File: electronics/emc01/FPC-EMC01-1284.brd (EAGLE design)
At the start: 100 x 86.6 mm, 52 parts, among them IC1 FT232RL, J10 ICSP, J11 CONN-RECT-16PIN-2ROW, J12 CONN-RECT-16PIN-2ROW, J13 CONN-RECT-16PIN-2ROW, J14 CONN-RECT-16PIN-2ROW, J2 PCIE, J4 MOT-X, J5 MOT-Y, J6 MOT-Z, J7 CONN-RECT-3PINJST_PH_2MM, J8 CONN-RECT-3PINJST_PH_2MM, J9 CONN-RECT-3PINJST_PH_2MM, Q4 16Mhz, U1 STEPSTICK, U2 STEPSTICK, U3 STEPSTICK, U5 ATMEGA1284P-AU, U6 LM2576-D2T, X1 USB-MICROB

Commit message: some extra routing
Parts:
- moved LED2 72.7 mm to (55.9, 8.35), turned to 270 degrees
- moved R6 70.2 mm to (55.9, 10.2), turned to 0 degrees
- moved JP5 1.60 mm to (90.9, 50.2)
- moved C18 1.57 mm to (84.2, 49.4)
- moved C36 0.86 mm to (39.1, 52.0)
- moved C34 0.70 mm to (39.2, 49.8)
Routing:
- net TOOL4_AIN: track 0.00 -> 125.6 mm, vias 0 -> 2
- net TOOL4_ENABLE: track 0.00 -> 84.0 mm, vias 0 -> 2
- net !RESET: track 90.8 -> 145.1 mm, vias 3 -> 4
- net SCLK: track 19.7 -> 73.6 mm, vias 0 -> 2
- net TOOL_DIR: track 27.6 -> 80.4 mm, vias 0 -> 3
- net TOOL4_DOUT: track 0.00 -> 40.1 mm, vias 0 -> 3
- net SDA: track 101.8 -> 133.5 mm
- net MISO: track 46.0 -> 76.4 mm, vias 1 -> 2
- net TOOL3_AIN: track 22.2 -> 52.5 mm, vias 1 -> 3
- net !XYZ-ENABLE: track 23.7 -> 44.9 mm, vias 0 -> 1
- net SCL: track 163.7 -> 181.7 mm, vias 3 -> 4
- net TOOL1_AIN: track 0.00 -> 3.78 mm
- net 12V: track 221.9 -> 219.8 mm
- net N$2: track 0.00 -> 1.91 mm
- net AVR_TXD: track 138.6 -> 139.9 mm
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
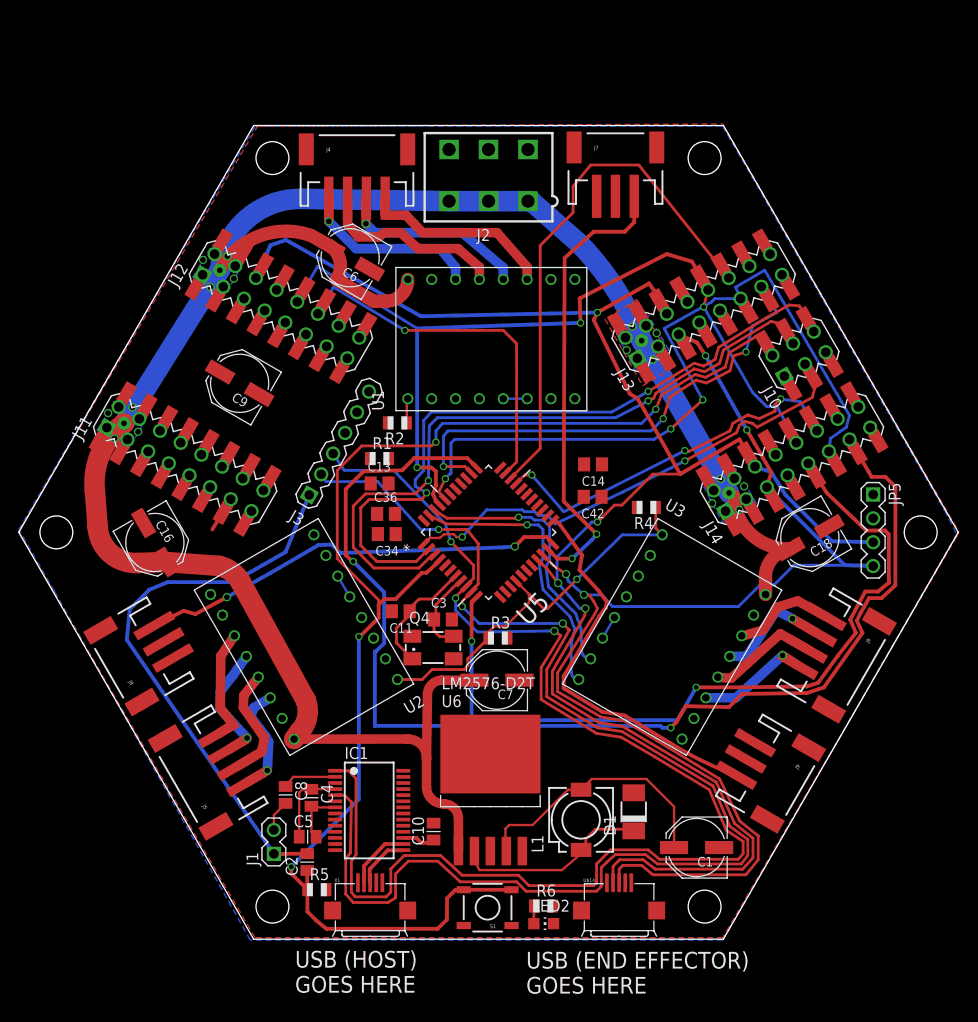
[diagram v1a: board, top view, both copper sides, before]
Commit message: - Swapped FT232RL for FT231XS (copied/pasted to Sparkfun RedBoard) - Replaced micro USB with mini USB - Deleted second micro USB and Z probe pin (we can use a modular connector Z probe instead rather than having a special connector for it)
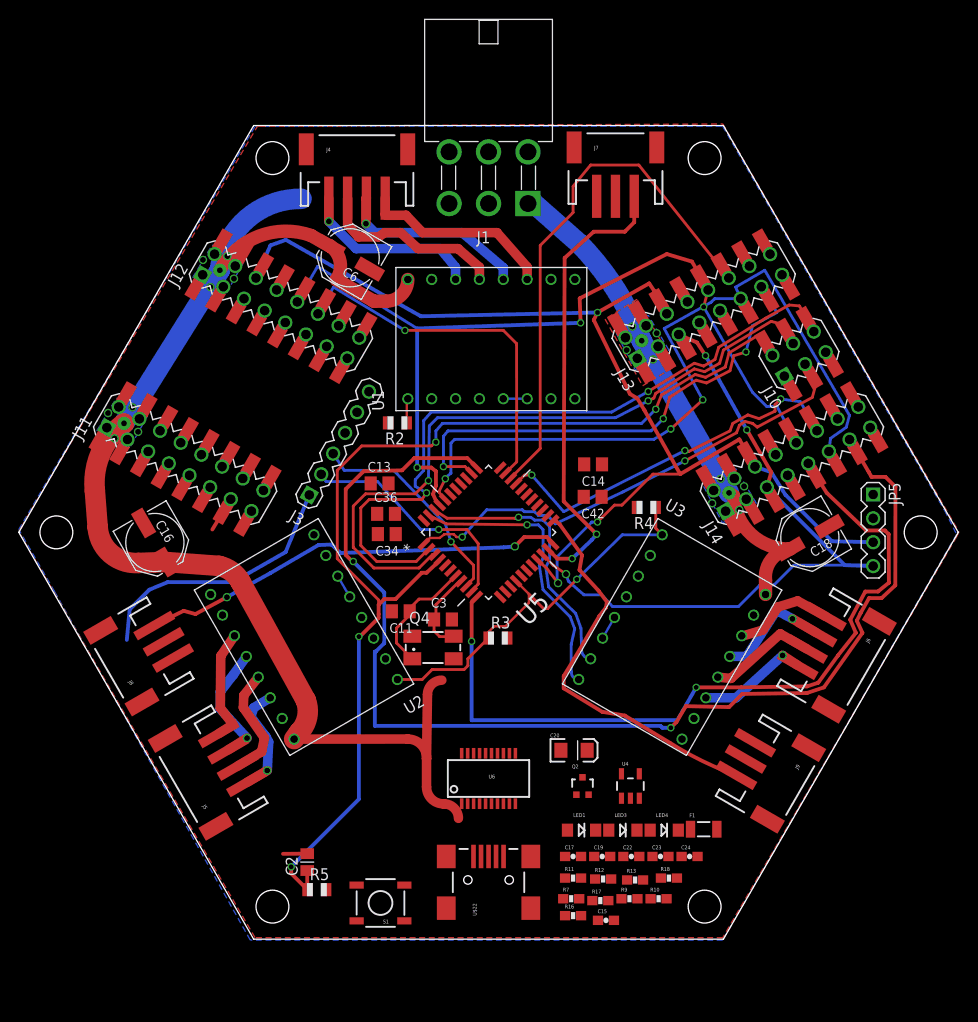
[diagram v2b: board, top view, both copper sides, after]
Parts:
- removed C1: 470uF, rcl:PANASONIC_D
- removed C10, C5, C8: 0.1uF, ipc-7351-capacitor:CAPC2012X145AN
- removed C4: 0.33uF, ipc-7351-capacitor:CAPC2012X145AN
- removed C7, C9: 100uF, rcl:PANASONIC_D
- removed D1: (no value), diode:DO-214AC
- removed IC1: FT232RL, ftdichip:SSOP28
- removed J2: PCIE, printrbot:5566-6
- removed L1: SLF7045, inductors:SLF7045
- removed LED2: PWR, led:CHIP-LED0805
- removed R1: 10K, adafruit:R0805
- removed R6: 330, adafruit:R0805
- removed U$14: USB-MICROB-I2CUSB-, SparkFun:USB-MICROB-I2C
- removed X1: USB-MICROB, SparkFun:USB-MICROB
- added C15: 1uF, SparkFun:0603-CAP
- added C17, C19, C24: 0.1uF, SparkFun:0603-CAP
- added C20: 10uF, SparkFun-Capacitors:EIA3216
- added C22, C23: 47pF, SparkFun-Capacitors:0603-CAP
- added F1: 500mA, SparkFun:PTC-1206
- added LED1: Green, SparkFun-LED:LED-1206-NO_SILK
- added LED3: Red, SparkFun-LED:LED-1206-NO_SILK
- added LED4: Yellow, SparkFun-LED:LED-1206-NO_SILK
- added Q2: 2N7002PW, SparkFun-DiscreteSemi:SOT323
- added R10, R11, R12, R7, R9: 1k, SparkFun:0603-RES
- added R13, R16: 27, SparkFun-Resistors:0603-RES
- added R17, R18: 10k, SparkFun:0603-RES
- added U$22: USB-MINIB-5PIN, SparkFun-Connectors:USB-MINIB
- added U4: MIC5205, SparkFun:SOT23-5
- J1: value (none) -> CONN-MOLEX-MICROFIT-6PIN; device !con-lstb:MA02-1 -> FirePick:CONN-MOLEX-MINIFIT-6PIN-2ROW
- U6: value LM2576-D2T -> FT231XS; device FirePick:D2PAK -> SparkFun-DigitalIC:SSOP20_L
- moved J1 71.7 mm to (50.0, 85.0), turned to 0 degrees
- moved S1 11.4 mm to (38.5, 10.6)
- moved U6 2.61 mm to (50.0, 23.8)
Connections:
- removed net N$10: C8.2, J1.2
- removed net N$12: C10.1, IC1.17
- removed net N$2: LED2.A, R6.1
- removed net N$3: C8.1, IC1.2
- removed net N$5: C1.+, L1.2, U6.4
- removed net USB_D+: IC1.15, X1.D+
- removed net USB_D-: IC1.16, X1.D-
- removed net Z-PROBE: R1.2, U5.44
- new net 3.3V: C15.1, C24.1, Q2.1, R17.2, U4.5, U6.13, U6.14, U6.3
- new net D+: C22.1, R16.1, U$22.D+
- new net D-: C23.1, R13.1, U$22.D-
- new net N$21: LED3.A, R9.2
- new net N$22: LED4.A, R10.2
- new net N$23: R13.2, U6.12
- new net N$25: R16.2, U6.11
- new net N$26: Q2.2, R17.1, U6.1
- new net RESERVED: U5.44
- new net RXD: R12.2, U6.4
- new net RXLED: LED4.C, U6.17
- new net TXD: R11.2, U6.20
- new net TXLED: LED3.C, U6.10
- new net VUSB: C17.1, F1.1, U$22.VBUS
- net +5V: now also C19.1, C20.A, F1.2, R10.1, R18.2, R7.2, R9.1, U4.1, U4.3, U6.15; no longer C4.1, C5.1, IC1.20, IC1.4, R1.1, R6.2, U$14.+5V
- net 12V: now also J1.1, J1.2, J1.3; no longer C7.+, C9.+, J2.1, J2.2, J2.3, U6.1
- net AVR_RXD: now also R11.1; no longer IC1.1
- net AVR_TXD: now also R12.1; no longer IC1.5
- net DTR: now also Q2.3, R18.1; no longer J1.1
- net GND: now also C15.2, C17.2, C19.2, C20.C, C22.2, C23.2, C24.2, J1.4, J1.5, J1.6, LED1.C, U$22.GND, U$22.MTN1, U$22.MTN2, U$22.MTN3, U$22.MTN4, U4.2, U6.16; no longer C1.-, C10.2, C4.2, C5.2, C7.-, C9.-, D1.A, IC1.18, IC1.21, IC1.25, IC1.26, IC1.7, J2.4, J2.5, J2.6, LED2.C, U$14.GND, U6.3, U6.5, X1.GND
- net N$4: now also LED1.A, R7.1; no longer D1.C, L1.1, U6.2
- net SCL: no longer U$14.SCL
- net SDA: no longer U$14.SDA
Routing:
- net AVR_RXD: track 139.4 -> 23.3 mm, vias 3 -> 1
- net AVR_TXD: track 139.9 -> 25.5 mm, vias 3 -> 1
- net SCL: track 181.7 -> 120.4 mm, vias 4 -> 3
- net SDA: track 133.5 -> 73.9 mm, vias 4 -> 3
- net 12V: track 219.8 -> 188.4 mm
- net DTR: track 59.5 -> 30.9 mm
- net N$5: track 28.1 -> 0.00 mm
- net !RESET: track 145.1 -> 117.3 mm
- net N$4: track 21.6 -> 0.00 mm
- net +5V: track 8.68 -> 0.00 mm
- net USB_D-: track 6.97 -> 0.00 mm
- net GND: track 6.03 -> 0.00 mm
- net USB_D+: track 5.91 -> 0.00 mm
- net N$3: track 5.77 -> 0.00 mm
- net N$12: track 3.58 -> 0.00 mm
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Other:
- board text removed: "USB (END EFFECTOR) GOES HERE"
- board text removed: "USB (HOST) GOES HERE"

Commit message: saving intermediate
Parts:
- moved C24 41.2 mm to (30.6, 21.4), turned to 180 degrees
- moved R18 37.6 mm to (31.8, 9.70)
- moved R12 33.0 mm to (30.7, 23.1)
- moved R17 32.5 mm to (30.6, 19.6)
- moved Q2 30.9 mm to (30.7, 13.1), turned to 180 degrees
- moved C23 24.6 mm to (44.8, 22.7), turned to 180 degrees
- moved F1 24.0 mm to (48.9, 19.8), turned to 90 degrees
- moved R13 23.7 mm to (44.8, 24.4), turned to 180 degrees
- moved C22 20.8 mm to (44.8, 19.6), turned to 180 degrees
- moved R11 19.1 mm to (44.8, 26.0), turned to 180 degrees
- moved R16 18.6 mm to (44.8, 21.2), turned to 180 degrees
- moved C15 17.4 mm to (55.1, 24.4)
- moved R10 15.0 mm to (61.1, 24.3), turned to 180 degrees
- moved C17 14.4 mm to (44.8, 18.0), turned to 180 degrees
- moved U6 12.5 mm to (37.9, 20.7), turned to 270 degrees
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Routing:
- net !RESET: track 117.3 -> 0.09 mm, vias 4 -> 0
- net 12V: track 188.4 -> 156.6 mm
- net DTR: track 30.9 -> 28.3 mm
- removed copper zone on layer 16, net GND

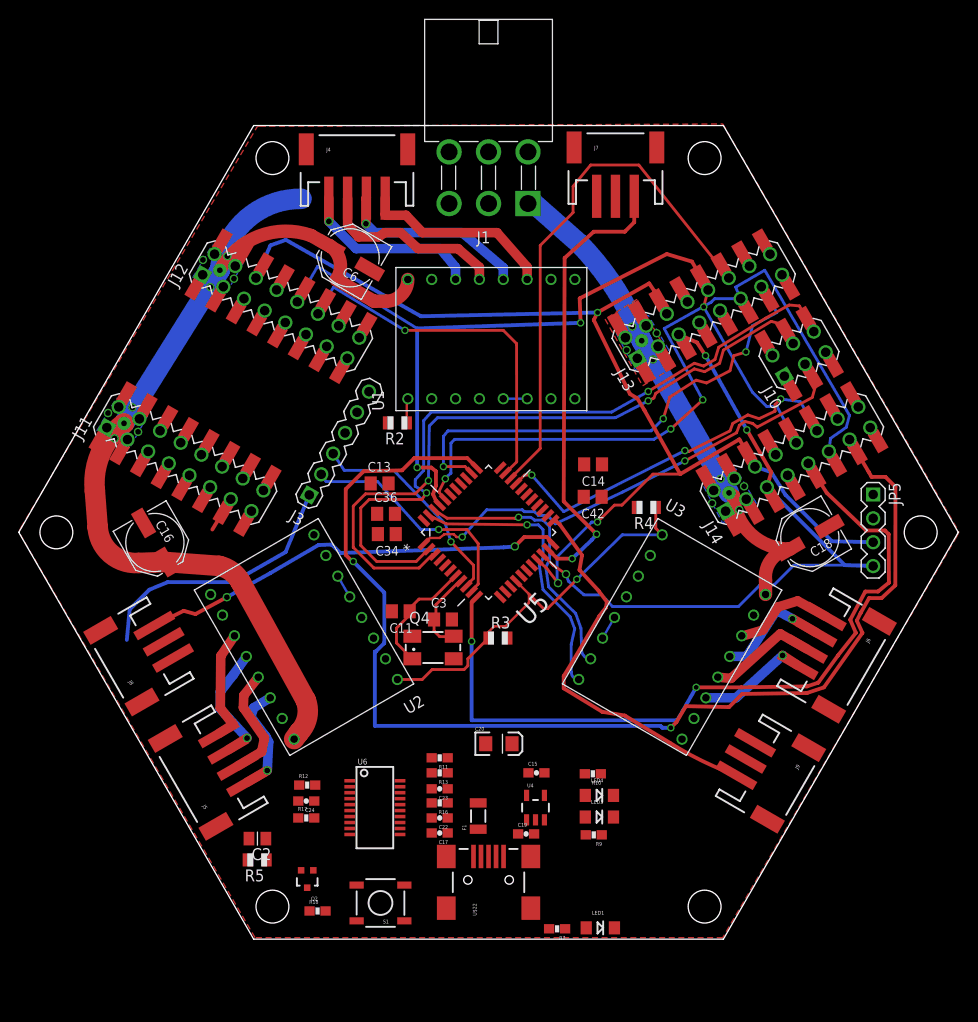
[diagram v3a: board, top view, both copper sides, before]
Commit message: autorouting v1
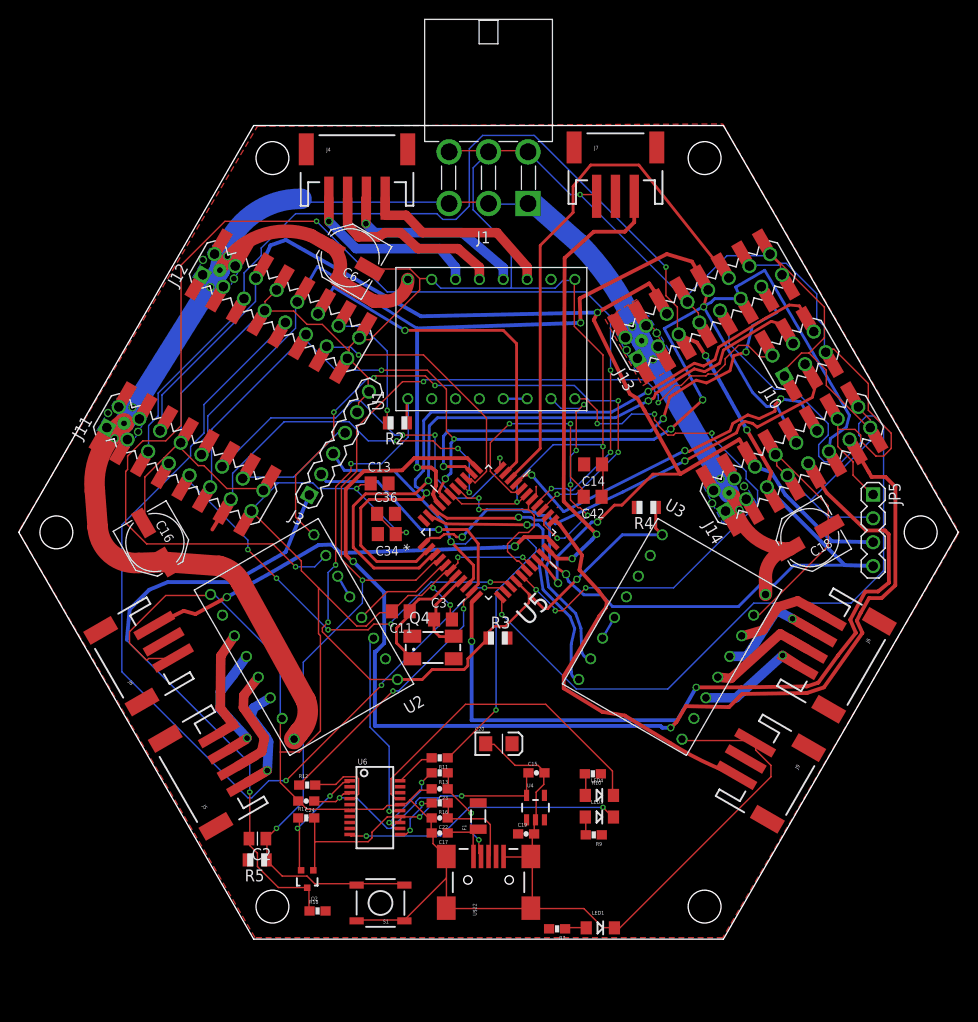
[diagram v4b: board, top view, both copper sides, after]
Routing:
- net GND: track 0.00 -> 549.1 mm, vias 0 -> 9
- net Y_DIR: track 0.00 -> 131.8 mm, vias 0 -> 5
- net !RESET: track 0.09 -> 128.6 mm, vias 0 -> 4
- net +5V: track 0.00 -> 127.2 mm, vias 0 -> 4
- net TOOL2_ENABLE: track 0.00 -> 100.3 mm, vias 0 -> 3
- net TOOL3_ENABLE: track 0.00 -> 99.6 mm, vias 0 -> 1
- net SDA: track 73.9 -> 166.3 mm, vias 3 -> 4
- net Y_STEP: track 0.00 -> 64.7 mm, vias 0 -> 6
- net X_STEP: track 0.00 -> 59.4 mm, vias 0 -> 6
- net 3.3V: track 0.00 -> 51.4 mm, vias 0 -> 3
- net TOOL1_ENABLE: track 0.00 -> 44.4 mm, vias 0 -> 5
- net TOOL_DIR: track 80.4 -> 124.6 mm, vias 3 -> 5
- net TOOL1_DOUT: track 0.00 -> 42.9 mm, vias 0 -> 3
- net !XYZ-ENABLE: track 44.9 -> 85.6 mm, vias 1 -> 4
- net DTR: track 28.3 -> 67.1 mm, vias 0 -> 1
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
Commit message: autorouting v2 w/ groundplane
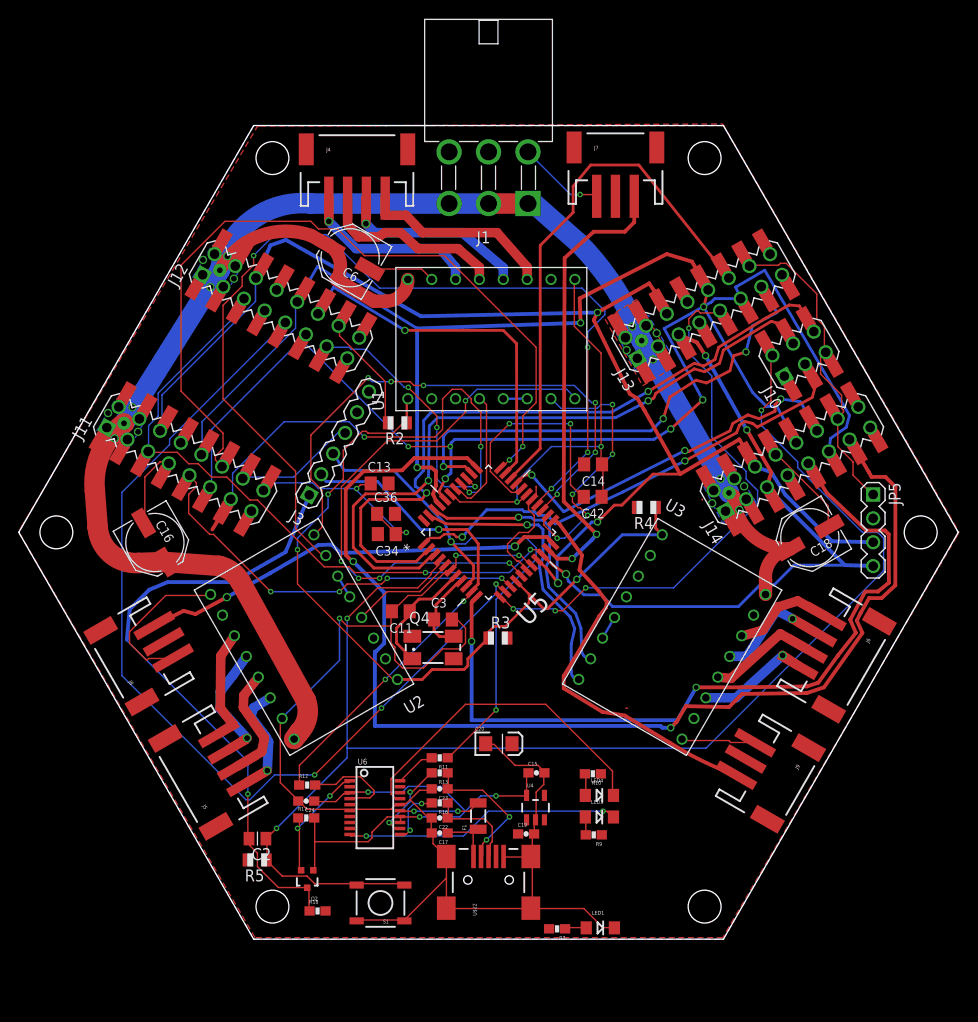
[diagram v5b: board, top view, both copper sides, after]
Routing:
- net GND: track 549.1 -> 280.2 mm, vias 9 -> 8
- net TOOL1_DOUT: track 42.9 -> 83.7 mm, vias 3 -> 2
- net TOOL3_ENABLE: track 99.6 -> 59.3 mm, vias 1 -> 4
- net Y_DIR: track 131.8 -> 103.5 mm, vias 5 -> 4
- net !RESET: track 128.6 -> 152.9 mm, vias 4 -> 3
- net SDA: track 166.3 -> 143.1 mm, vias 4 -> 5
- net +5V: track 127.2 -> 105.3 mm, vias 4 -> 2
- net TOOL1_AIN: track 40.5 -> 52.1 mm
- net Y_STEP: track 64.7 -> 59.2 mm
- net D-: track 10.4 -> 15.1 mm
- net X_DIR: track 24.8 -> 28.9 mm
- net RXD: track 7.82 -> 10.4 mm
- net TOOL_DIR: track 124.6 -> 122.3 mm
- net TOOL2_AIN: track 28.7 -> 27.2 mm, vias 1 -> 3
- net !XYZ-ENABLE: track 85.6 -> 84.2 mm, vias 4 -> 3
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- added copper zone on layer 16, net GND
